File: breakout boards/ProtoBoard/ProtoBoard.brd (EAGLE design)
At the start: 25 x 25 mm, 3 parts

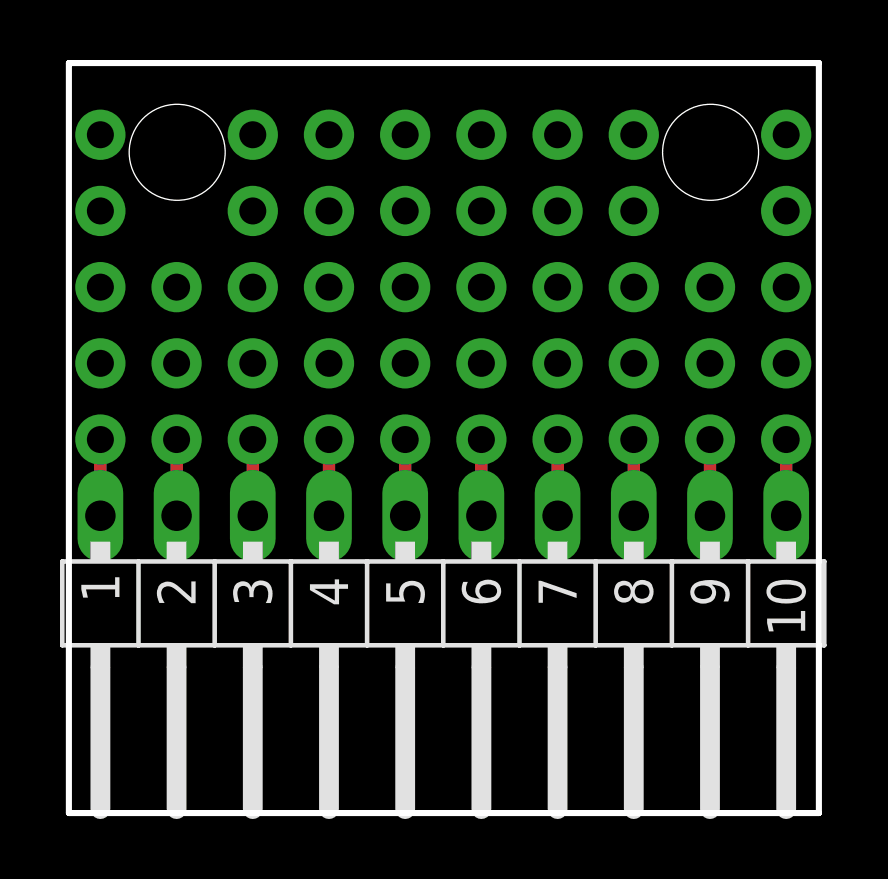
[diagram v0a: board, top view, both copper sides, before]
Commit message: updated breakout boards
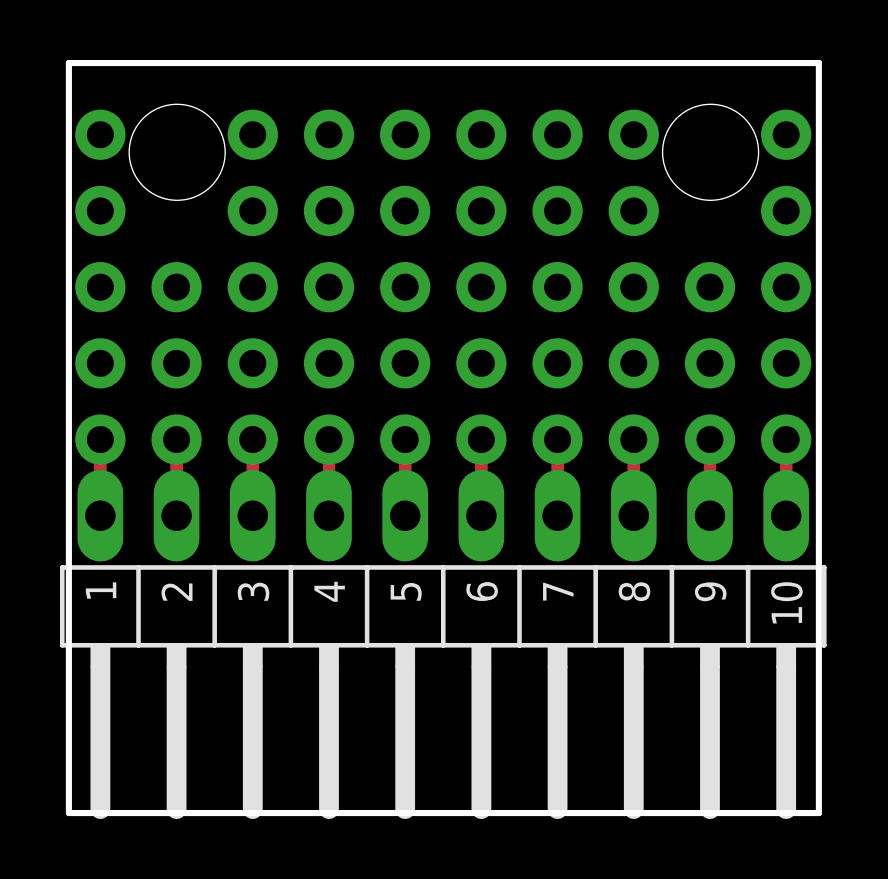
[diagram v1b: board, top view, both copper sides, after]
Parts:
- JP1: device theairboard:SIL-1X10 -> TheAirBoard_breakouts:SIL10-2.54MM
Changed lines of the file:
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@@
 </plain>
 <attributes>
-<attribute name="DESIGNER" value="theairboard.cc"/>
+<attribute name="DESIGNER" value="AirThings Inc"/>
 <attribute name="REV" value="1.0"/>
 <attribute name="SENSOR" value=""/>
@@
 </autorouter>
 <elements>
-<element name="JP1" library="theairboard" package="SIL-1X10" value="SIL" x="49.53" y="33.02" smashed="yes" rot="R180">
+<element name="JP1" library="TheAirBoard_breakouts" package="SIL10-2.54MM" value="SIL" x="49.53" y="33.02" smashed="yes" rot="R180">
 <attribute name="OC_NEWARK" value="93K5133" x="22.86" y="69.85" size="1.778" layer="27" rot="R180" display="off"/>
 <attribute name="MANUFACTURER" value="FCI" x="22.86" y="69.85" size="1.778" layer="27" rot="R180" display="off"/>
